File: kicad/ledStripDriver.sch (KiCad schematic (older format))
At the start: 57 parts, among them J1 AudioJack3_SwitchTR, J2 USB_POWER_OUT, K1 G5RL1AELN5DC, Q1 Q_NPN_BEC_S8050, Q2 AO3400, Q3 AO3400, Q4 AO3400, SW1 SW_DIP_x01, SW2 Rotary_Encoder_Switch, SW3 SW_Push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

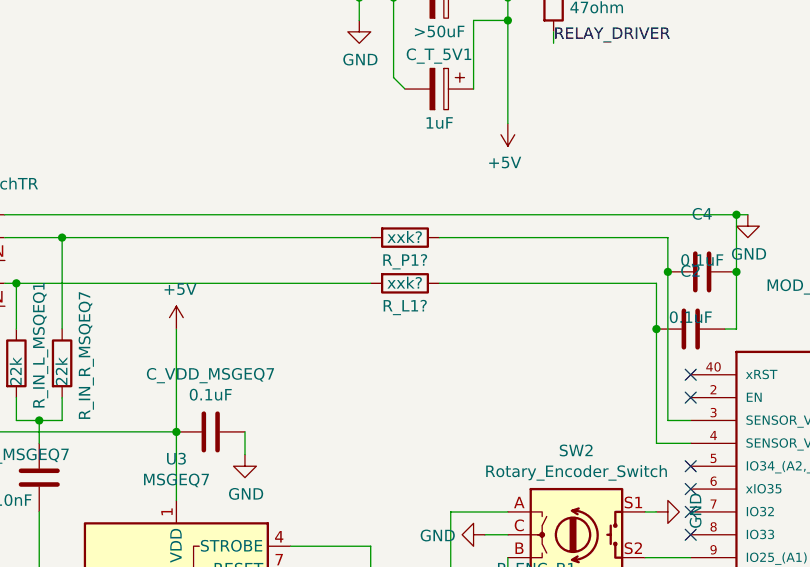
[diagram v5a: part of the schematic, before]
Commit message: With charging port.
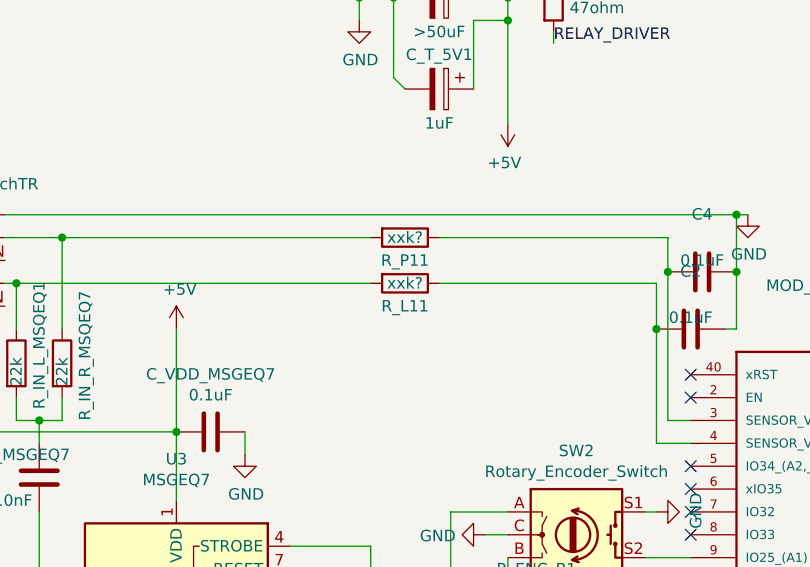
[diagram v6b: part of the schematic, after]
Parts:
- D1, D2, D3: footprint Diode_SMD:D_SMA_Handsoldering -> ptabOther:D_SMA_Handsoldering
- gave numbers to parts that had none: 2
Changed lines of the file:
@@
 F 0 "D1" V 2454 2279 50  0000 L CNN
 F 1 "D_Schottky_SS14" V 2545 2279 50  0000 L CNN
-F 2 "Diode_SMD:D_SMA_Handsoldering" H 2500 2200 50  0001 C CNN
+F 2 "ptabOther:D_SMA_Handsoldering" H 2500 2200 50  0001 C CNN
 F 3 "~" H 2500 2200 50  0001 C CNN
 	1    2500 2200
@@
 F 0 "D3" H 3700 3166 50  0000 C CNN
 F 1 "M1" H 3700 3075 50  0000 C CNN
-F 2 "Diode_SMD:D_SMA_Handsoldering" H 3700 2950 50  0001 C CNN
+F 2 "ptabOther:D_SMA_Handsoldering" H 3700 2950 50  0001 C CNN
 F 3 "~" H 3700 2950 50  0001 C CNN
 	1    3700 2950
@@
 F 0 "D2" V 4796 4221 50  0000 R CNN
 F 1 "D_Schottky_SS14" V 4705 4221 50  0000 R CNN
-F 2 "Diode_SMD:D_SMA_Handsoldering" H 4750 4300 50  0001 C CNN
+F 2 "ptabOther:D_SMA_Handsoldering" H 4750 4300 50  0001 C CNN
 F 3 "~" H 4750 4300 50  0001 C CNN
 	1    4750 4300
@@
 $EndComp
 $Comp
-L Device:R R_P1?
+L Device:R R_P11
 U 1 1 5F615C3F
 P 2700 4450
-F 0 "R_P1?" V 2800 4450 50  0000 C CNN
+F 0 "R_P11" V 2800 4450 50  0000 C CNN
 F 1 "xxk?" V 2700 4450 50  0000 C CNN
 F 2 "Resistor_SMD:R_0805_2012Metric_Pad1.15x1.40mm_HandSolder" V 2630 4450 50  0001 C CNN
@@
 $EndComp
 $Comp
-L Device:R R_L1?
+L Device:R R_L11
 U 1 1 5F6197B4
 P 2700 4650
-F 0 "R_L1?" V 2800 4650 50  0000 C CNN
+F 0 "R_L11" V 2800 4650 50  0000 C CNN
 F 1 "xxk?" V 2700 4650 50  0000 C CNN
 F 2 "Resistor_SMD:R_0805_2012Metric_Pad1.15x1.40mm_HandSolder" V 2630 4650 50  0001 C CNN

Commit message: v3 - working and split between files. StroboRainbows.
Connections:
- wire segments 185 -> 190
- no-connect marks 25 -> 23
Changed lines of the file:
@@
 $EndComp
 Wire Wire Line
-	9350 2850 9350 2900
+	9350 2700 9350 2900
 Wire Wire Line
 	9350 3200 9350 3300
@@
 $EndComp
 Wire Wire Line
-	9350 3800 9350 3850
+	9350 3550 9350 3850
 Wire Wire Line
 	9350 4150 9350 4250
@@
 $EndComp
 Wire Wire Line
-	9350 4800 9350 4850
+	9350 4550 9350 4850
 Wire Wire Line
 	9350 5150 9350 5250
@@
 Wire Wire Line
 	6050 4400 6250 4400
-Text Label 9700 5150 1    50   ~ 0
+Text Label 9350 4650 0    50   ~ 0
 12V_POST_RELAY
 Text Label 9350 3700 0    50   ~ 0
@@
 NoConn ~ 3950 5450
 NoConn ~ 3950 5150
-NoConn ~ 5050 7150
-NoConn ~ 4900 7150
 NoConn ~ 3950 5050
 NoConn ~ 3950 5550
@@
 	1150 6700 1150 6900
 Wire Wire Line
-	4750 7150 4750 7450
+	4750 7150 4750 7250
 Wire Wire Line
 	950  4350 4150 4350
@@
 Wire Wire Line
 	3150 3500 3150 3950
+Wire Wire Line
+	5050 7150 5050 7250
+Wire Wire Line
+	5050 7250 4900 7250
+Wire Wire Line
+	4900 7250 4900 7150
+Wire Wire Line
+	4900 7250 4750 7250
+Connection ~ 4900 7250
+Connection ~ 4750 7250
+Wire Wire Line
+	4750 7250 4750 7450
 $EndSCHEMATC

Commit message: v4 - preprod
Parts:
- R_L2_12V1: renamed from R9; value R_L2_12V -> 300
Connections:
- wire segments 190 -> 197
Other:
- moved on the sheet: R_ENC_A1, R_ENC_B1
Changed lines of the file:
@@
 Wire Wire Line
 	6050 4400 6250 4400
-Text Label 9350 4650 0    50   ~ 0
-12V_POST_RELAY
 Text Label 9350 3700 0    50   ~ 0
 12V_POST_RELAY
@@
 	10000 5250 9650 5250
 $Comp
-L Device:R R9
+L Device:R R_L2_12V1
 U 1 1 5E7F5FB9
 P 9500 4250
-F 0 "R9" V 9500 4250 50  0000 C CNN
-F 1 "R_L2_12V" V 9400 4250 50  0000 C CNN
+F 0 "R_L2_12V1" V 9400 4250 50  0000 C CNN
+F 1 "300" V 9500 4250 50  0000 C CNN
 F 2 "Resistor_SMD:R_0805_2012Metric_Pad1.15x1.40mm_HandSolder" V 9430 4250 50  0001 C CNN
 F 3 "~" H 9500 4250 50  0001 C CNN
@@
 Wire Wire Line
 	2900 6050 2900 5650
-Wire Wire Line
-	3950 6050 3850 6050
 Wire Wire Line
 	3950 6000 3950 5950
@@
 L Device:R R_ENC_B1
 U 1 1 5F69D010
-P 3300 6000
-F 0 "R_ENC_B1" V 3200 5800 50  0000 L CNN
-F 1 "10k" V 3300 5950 50  0000 L CNN
-F 2 "Resistor_SMD:R_0805_2012Metric_Pad1.15x1.40mm_HandSolder" V 3230 6000 50  0001 C CNN
-F 3 "~" H 3300 6000 50  0001 C CNN
-	1    3300 6000
-	0    1    1    0
+P 2850 6850
+F 0 "R_ENC_B1" V 2750 6650 50  0000 L CNN
+F 1 "10k" V 2850 6800 50  0000 L CNN
+F 2 "Resistor_SMD:R_0805_2012Metric_Pad1.15x1.40mm_HandSolder" V 2780 6850 50  0001 C CNN
+F 3 "~" H 2850 6850 50  0001 C CNN
+	1    2850 6850
+	-1   0    0    1
 $EndComp
 $Comp
 L Device:R R_ENC_A1
 U 1 1 5F69DB04
-P 3700 6050
-F 0 "R_ENC_A1" V 3600 5850 50  0000 L CNN
-F 1 "10k" V 3700 5950 50  0000 L CNN
-F 2 "Resistor_SMD:R_0805_2012Metric_Pad1.15x1.40mm_HandSolder" V 3630 6050 50  0001 C CNN
-F 3 "~" H 3700 6050 50  0001 C CNN
-	1    3700 6050
-	0    1    1    0
+P 3600 6850
+F 0 "R_ENC_A1" V 3500 6650 50  0000 L CNN
+F 1 "10k" V 3600 6800 50  0000 L CNN
+F 2 "Resistor_SMD:R_0805_2012Metric_Pad1.15x1.40mm_HandSolder" V 3530 6850 50  0001 C CNN
+F 3 "~" H 3600 6850 50  0001 C CNN
+	1    3600 6850
+	-1   0    0    1
 $EndComp
 $Comp
@@
 Connection ~ 3450 7000
 Wire Wire Line
-	3450 7000 3650 7000
+	3450 7000 3600 7000
 Wire Wire Line
 	3650 6550 3650 7000
@@
 	2900 6050 3450 6050
 Wire Wire Line
-	3150 5850 3150 6000
-Connection ~ 3150 6000
-Wire Wire Line
-	3450 6000 3950 6000
-Wire Wire Line
-	3150 6000 3150 6650
-Wire Wire Line
-	3450 6050 3450 6650
+	3450 6050 3450 6350
 Connection ~ 3450 6050
-Wire Wire Line
-	3450 6050 3550 6050
 Connection ~ 1150 6400
 Wire Wire Line
@@
 Wire Wire Line
 	4750 7250 4750 7450
+Wire Wire Line
+	3150 5850 3150 6000
+Wire Wire Line
+	3450 6050 3950 6050
+Wire Wire Line
+	3150 6000 3950 6000
+Connection ~ 3150 6000
+Wire Wire Line
+	3150 6000 3150 6350
+Connection ~ 3600 7000
+Wire Wire Line
+	3600 7000 3650 7000
+Wire Wire Line
+	3600 6700 3600 6350
+Wire Wire Line
+	3600 6350 3450 6350
+Connection ~ 3450 6350
+Wire Wire Line
+	3450 6350 3450 6650
+Wire Wire Line
+	3150 7000 2850 7000
+Connection ~ 3150 7000
+Wire Wire Line
+	2850 6700 2850 6350
+Wire Wire Line
+	2850 6350 3150 6350
+Connection ~ 3150 6350
+Wire Wire Line
+	3150 6350 3150 6650
+Text Label 9350 4650 0    50   ~ 0
+12V_POST_RELAY
 $EndSCHEMATC
